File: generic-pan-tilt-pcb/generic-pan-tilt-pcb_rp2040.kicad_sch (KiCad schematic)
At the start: 28 parts, among them U1 RP2040, U2 W25Q128JVS, Y1 ABM8-272-T3

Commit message: fix all drc and erc
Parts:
- U1: footprint Package_DFN_QFN:QFN-56-1EP_7x7mm_P0.4mm_EP3.2x3.2mm -> generic-pan-tilt-pcb:RP2040_QFN-56-1EP_7x7mm_P0.4mm_EP3.2x3.2mm
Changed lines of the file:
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@@
 			)
 		)
-		(property "Footprint" "Package_DFN_QFN:QFN-56-1EP_7x7mm_P0.4mm_EP3.2x3.2mm"
+		(property "Footprint" "generic-pan-tilt-pcb:RP2040_QFN-56-1EP_7x7mm_P0.4mm_EP3.2x3.2mm"
 			(at 93.98 114.3 0)
 			(effects

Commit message: fix c footprint for r
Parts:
- R10, R11, R12, R13, R14, R6, R7, R8, R9: footprint Capacitor_SMD:C_0402_1005Metric -> Resistor_SMD:R_0402_1005Metric
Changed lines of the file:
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@@
 			)
 		)
-		(property "Footprint" "Capacitor_SMD:C_0402_1005Metric"
+		(property "Footprint" "Resistor_SMD:R_0402_1005Metric"
 			(at 39.624 85.344 90)
 			(effects
@@
 			)
 		)
-		(property "Footprint" "Capacitor_SMD:C_0402_1005Metric"
+		(property "Footprint" "Resistor_SMD:R_0402_1005Metric"
 			(at 39.624 82.804 90)
 			(effects
@@
 			)
 		)
-		(property "Footprint" "Capacitor_SMD:C_0402_1005Metric"
+		(property "Footprint" "Resistor_SMD:R_0402_1005Metric"
 			(at 194.056 113.284 90)
 			(effects
@@
 			)
 		)
-		(property "Footprint" "Capacitor_SMD:C_0402_1005Metric"
+		(property "Footprint" "Resistor_SMD:R_0402_1005Metric"
 			(at 59.944 131.064 90)
 			(effects
@@
 			)
 		)
-		(property "Footprint" "Capacitor_SMD:C_0402_1005Metric"
+		(property "Footprint" "Resistor_SMD:R_0402_1005Metric"
 			(at 195.834 72.644 90)
 			(effects
@@
 			)
 		)
-		(property "Footprint" "Capacitor_SMD:C_0402_1005Metric"
+		(property "Footprint" "Resistor_SMD:R_0402_1005Metric"
 			(at 63.246 71.374 90)
 			(effects
@@
 			)
 		)
-		(property "Footprint" "Capacitor_SMD:C_0402_1005Metric"
+		(property "Footprint" "Resistor_SMD:R_0402_1005Metric"
 			(at 233.934 82.804 90)
 			(effects
@@
 			)
 		)
-		(property "Footprint" "Capacitor_SMD:C_0402_1005Metric"
+		(property "Footprint" "Resistor_SMD:R_0402_1005Metric"
 			(at 233.934 72.644 90)
 			(effects
@@
 			)
 		)
-		(property "Footprint" "Capacitor_SMD:C_0402_1005Metric"
+		(property "Footprint" "Resistor_SMD:R_0402_1005Metric"
 			(at 195.834 82.804 90)
 			(effects

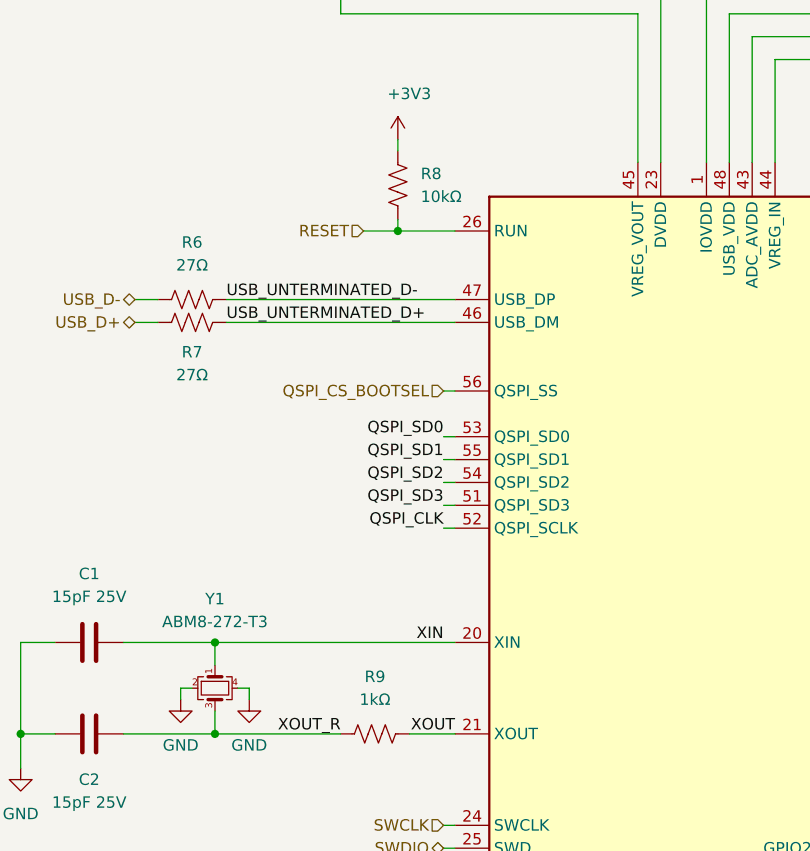
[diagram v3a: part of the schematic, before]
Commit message: 0603 caps for psu rs485
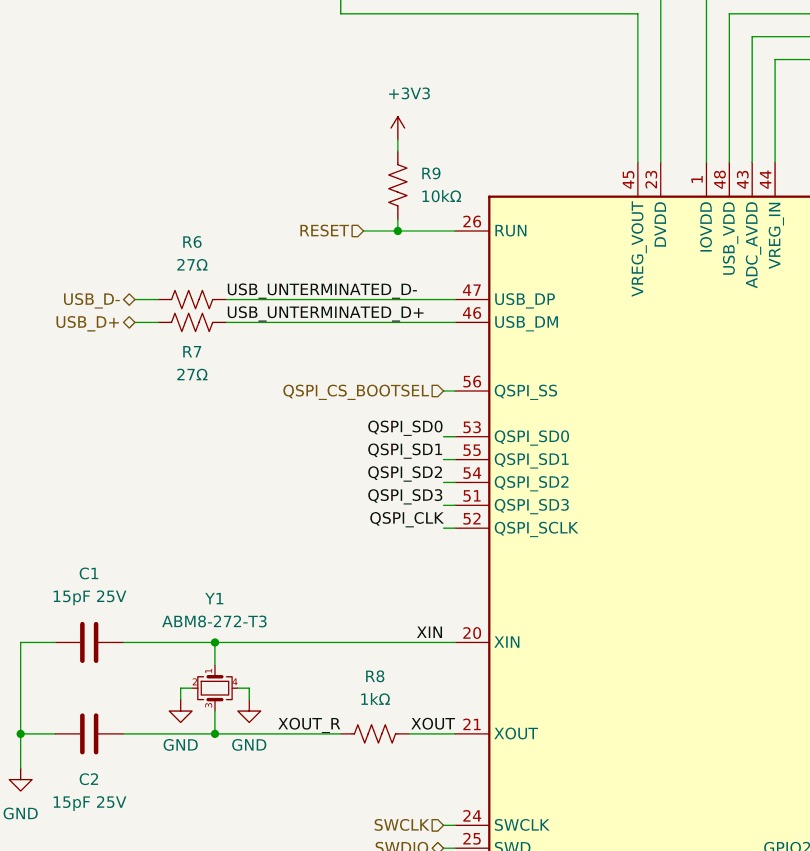
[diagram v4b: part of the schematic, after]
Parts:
- renumbered R9 to R8, R8 to R9
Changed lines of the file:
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@@
 		(dnp no)
 		(fields_autoplaced yes)
-		(property "Reference" "R9"
+		(property "Reference" "R8"
 			(at 59.69 125.73 90)
 			(effects
@@
 			(project "generic-pan-tilt-pcb"
 				(path "/e3bbbe58-bf8f-42a8-8505-028de8235dc1/55ec4a5b-72e0-465a-b2bf-185865323fab"
-					(reference "R9")
+					(reference "R8")
 					(unit 1)
 				)
@@
 		(dnp no)
 		(fields_autoplaced yes)
-		(property "Reference" "R8"
+		(property "Reference" "R9"
 			(at 64.77 69.8499 0)
 			(effects
@@
 			(project "generic-pan-tilt-pcb"
 				(path "/e3bbbe58-bf8f-42a8-8505-028de8235dc1/55ec4a5b-72e0-465a-b2bf-185865323fab"
-					(reference "R8")
-					(unit 1)
-				)
+					(reference "R9")
+					(unit 1)
+				)

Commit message: fix part numbers, add newark parts, separate fields for part desc
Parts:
- U1: newark# (none) -> 49AJ8739
- Y1: newark# (none) -> 86AK7198
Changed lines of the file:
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@@
+			)
+		)
+		(property "newark#" "49AJ8739"
+			(at 93.98 114.3 0)
+			(effects
+				(font
+					(size 1.27 1.27)
+				)
+				(hide yes)
 			)
 		)
@@
 			(at 41.91 127 0)
 			(effects
+				(font
+					(size 1.27 1.27)
+				)
+				(hide yes)
+			)
+		)
+		(property "newark#" "86AK7198"
+			(at 41.91 127 0)
+			(effects

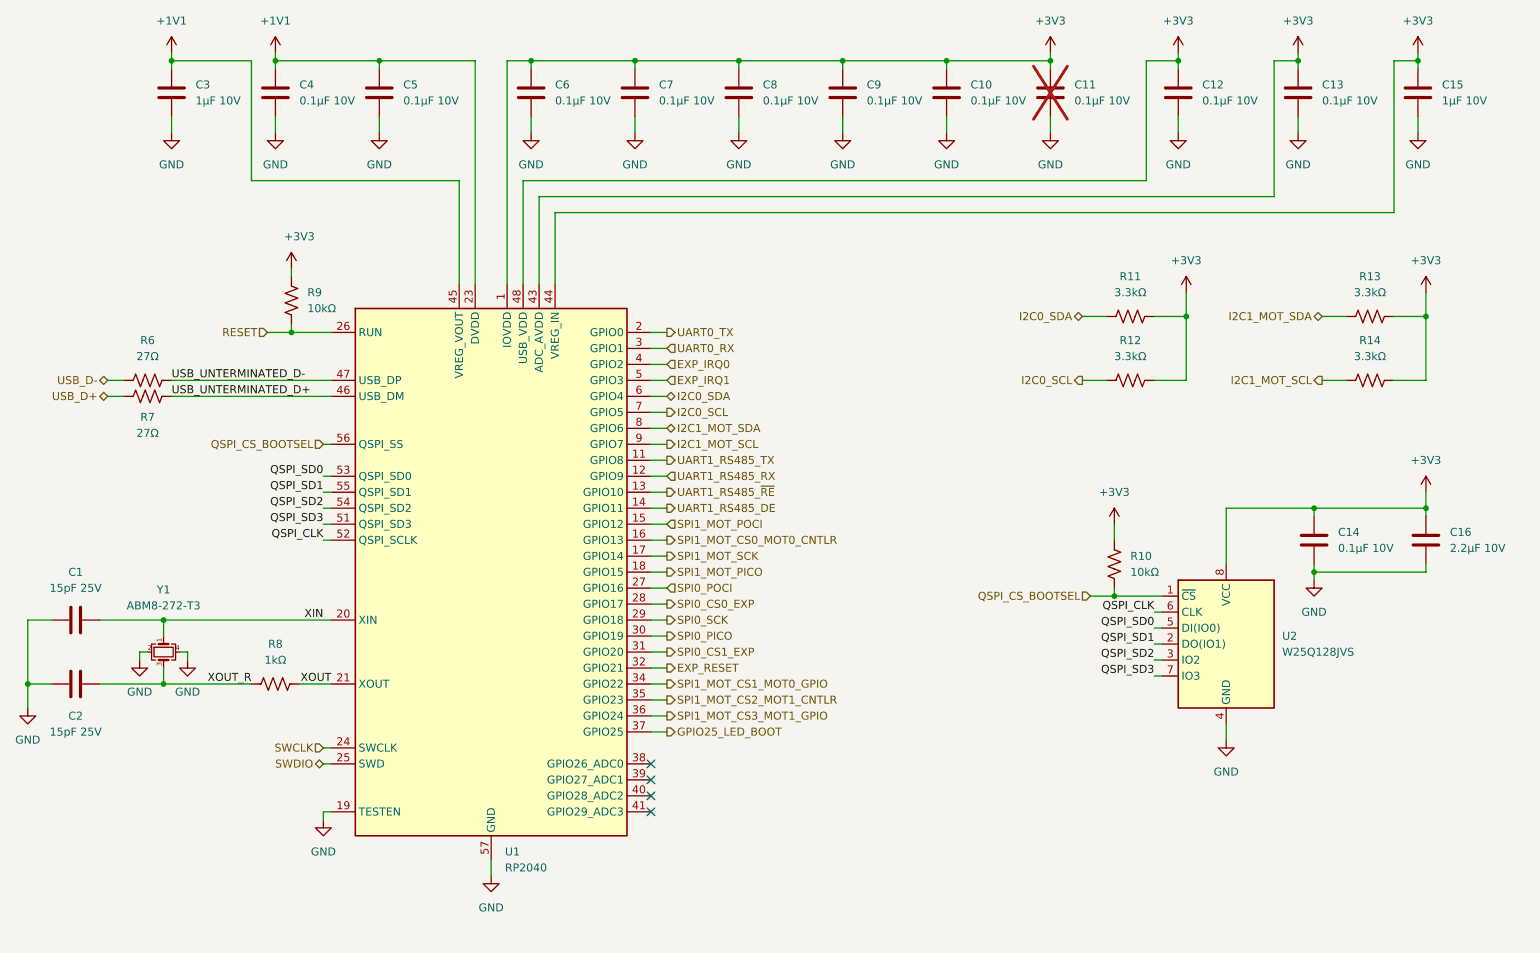
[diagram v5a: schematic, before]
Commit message: main board fix usb, fix uart, all caps and resistors manf and vendor, sch only replace psu and accel caps
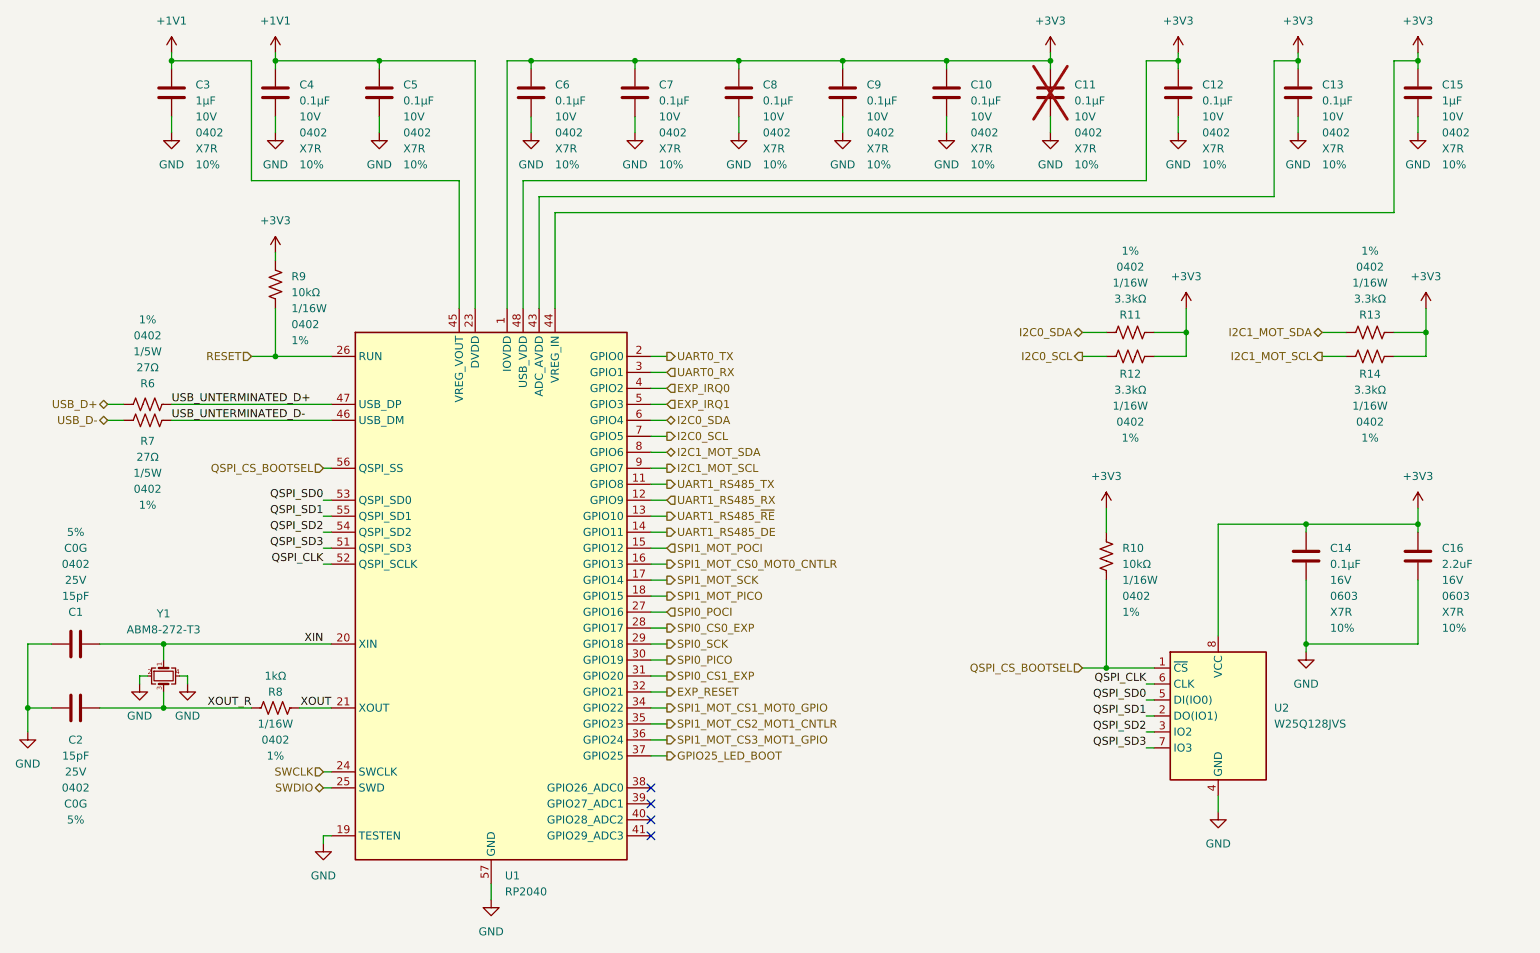
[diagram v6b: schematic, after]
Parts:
- C1, C2: value 15pF 25V -> 15pF; Case Code (none) -> 0402; Dielectric (none) -> C0G; Tolerance (none) -> 5%; Voltage (none) -> 25V; digikey# (none) -> 311-3746-1-ND; lcsc# (none) -> C541359; manf# (none) -> CC0402JRNPO8BN150; mouser# (none) -> 603-CC402JRNPO8BN150; newark# (none) -> 80AK9023
- C10, C11, C12, C13, C4, C5, C6, C7, C8, C9: value 0.1µF 10V -> 0.1µF; Case Code (none) -> 0402; Dielectric (none) -> X7R; Tolerance (none) -> 10%; Voltage (none) -> 10V; digikey# (none) -> 1276-1002-1-ND; lcsc# (none) -> C133086; manf# (none) -> CL05B104KP5NNNC; mouser# (none) -> 187-CL05B104KP5NNNC; newark# (none) -> 82AC9219
- C14: value 0.1µF 10V -> 0.1µF; footprint Capacitor_SMD:C_0402_1005Metric -> Capacitor_SMD:C_0603_1608Metric; Case Code (none) -> 0603; Dielectric (none) -> X7R; Tolerance (none) -> 10%; Voltage (none) -> 16V; digikey# (none) -> 1276-1005-1-ND; lcsc# (none) -> C66501; manf# (none) -> CL10B104KO8NNNC; mouser# (none) -> 187-CL10B104KO8NNNC; newark# (none) -> 82AC9325
- C15, C3: value 1µF 10V -> 1µF; Case Code (none) -> 0402; Dielectric (none) -> X7R; Tolerance (none) -> 10%; Voltage (none) -> 10V; digikey# (none) -> 490-GRM155Z71A105KE01JCT-ND; lcsc# (none) -> C528974; manf# (none) -> GRM155Z71A105KE01; mouser# (none) -> 81-GRM155Z71A105KE1J; newark# (none) -> 63AK6703
- C16: value 2.2µF 10V -> 2.2uF; footprint Capacitor_SMD:C_0402_1005Metric -> Capacitor_SMD:C_0603_1608Metric; Case Code (none) -> 0603; Dielectric (none) -> X7R; Tolerance (none) -> 10%; Voltage (none) -> 16V; digikey# (none) -> 490-GRM188Z71C225KE43DCT-ND; lcsc# (none) -> C576485; manf# (none) -> GRM188Z71C225KE43D; mouser# (none) -> 81-­GRM188Z71C225KE3D; newark# (none) -> 92AH5122
- R10, R9: Case Code (none) -> 0402; Power (none) -> 1/16W; Tolerance (none) -> 1%; digikey# (none) -> CR0402-FX-1002GLFCT-ND; lcsc# (none) -> C202396; manf# (none) -> CR0402-FX-1002GLF; mouser# (none) -> 652-CR0402FX-1002GLF; newark# (none) -> 06X5113
- R11, R12, R13, R14: Case Code (none) -> 0402; Power (none) -> 1/16W; Tolerance (none) -> 1%; digikey# (none) -> CR0402-FX-3301GLFCT-ND; lcsc# (none) -> C2077176; manf# (none) -> CR0402-FX-3301GLF; mouser# (none) -> 652-CR0402FX-3301GLF; newark# (none) -> 33AK7350
- R6, R7: Case Code (none) -> 0402; Power (none) -> 1/5W; Tolerance (none) -> 1%; digikey# (none) -> 541-10398-1-ND; lcsc# (none) -> C2100055; manf# (none) -> RCS040227R0FKED; mouser# (none) -> 71-RCS040227R0FKED; newark# (none) -> 41AH4918
- R8: Case Code (none) -> 0402; Power (none) -> 1/16W; Tolerance (none) -> 1%; digikey# (none) -> CR0402-FX-1001GLFCT-ND; lcsc# (none) -> C202394; manf# (none) -> CR0402-FX-1001GLF; mouser# (none) -> 652-CR0402FX-1001GLF; newark# (none) -> 02J1761
- U1: lcsc# (none) -> C3227924
- U2: lcsc# (none) -> C97521
- Y1: lcsc# (none) -> C20625731
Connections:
- net +3V3: now also R11.1, R13.1; no longer R11.2, R13.2
- net GND: now also C1.2; no longer C1.1
- net I2C0_SDA: now also R11.2; no longer R11.1
- net I2C1_MOT_SDA: now also R13.2; no longer R13.1
- net USB_D+: now also R6.2; no longer R7.1
- net USB_D-: now also R7.1; no longer R6.1
- net USB_UNTERMINATED_D+: now also R6.1, U1.47 (USB_DP); no longer R7.2, U1.46 (USB_DM)
- net USB_UNTERMINATED_D-: now also R7.2, U1.46 (USB_DM); no longer R6.2, U1.47 (USB_DP)
- net XIN: now also C1.1; no longer C1.2
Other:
- moved on the sheet: C2, R12, R7, U1, U2, Y1
